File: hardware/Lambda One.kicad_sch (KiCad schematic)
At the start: 35 parts, among them IC1 DS1818, J1 Conn_01x02, SW1 SW_Push, U1 W65C816SxP, U12 74HC245, U3 ATF22LV10C, U8 74HC00, U9 74HC00, Y1 TFT680

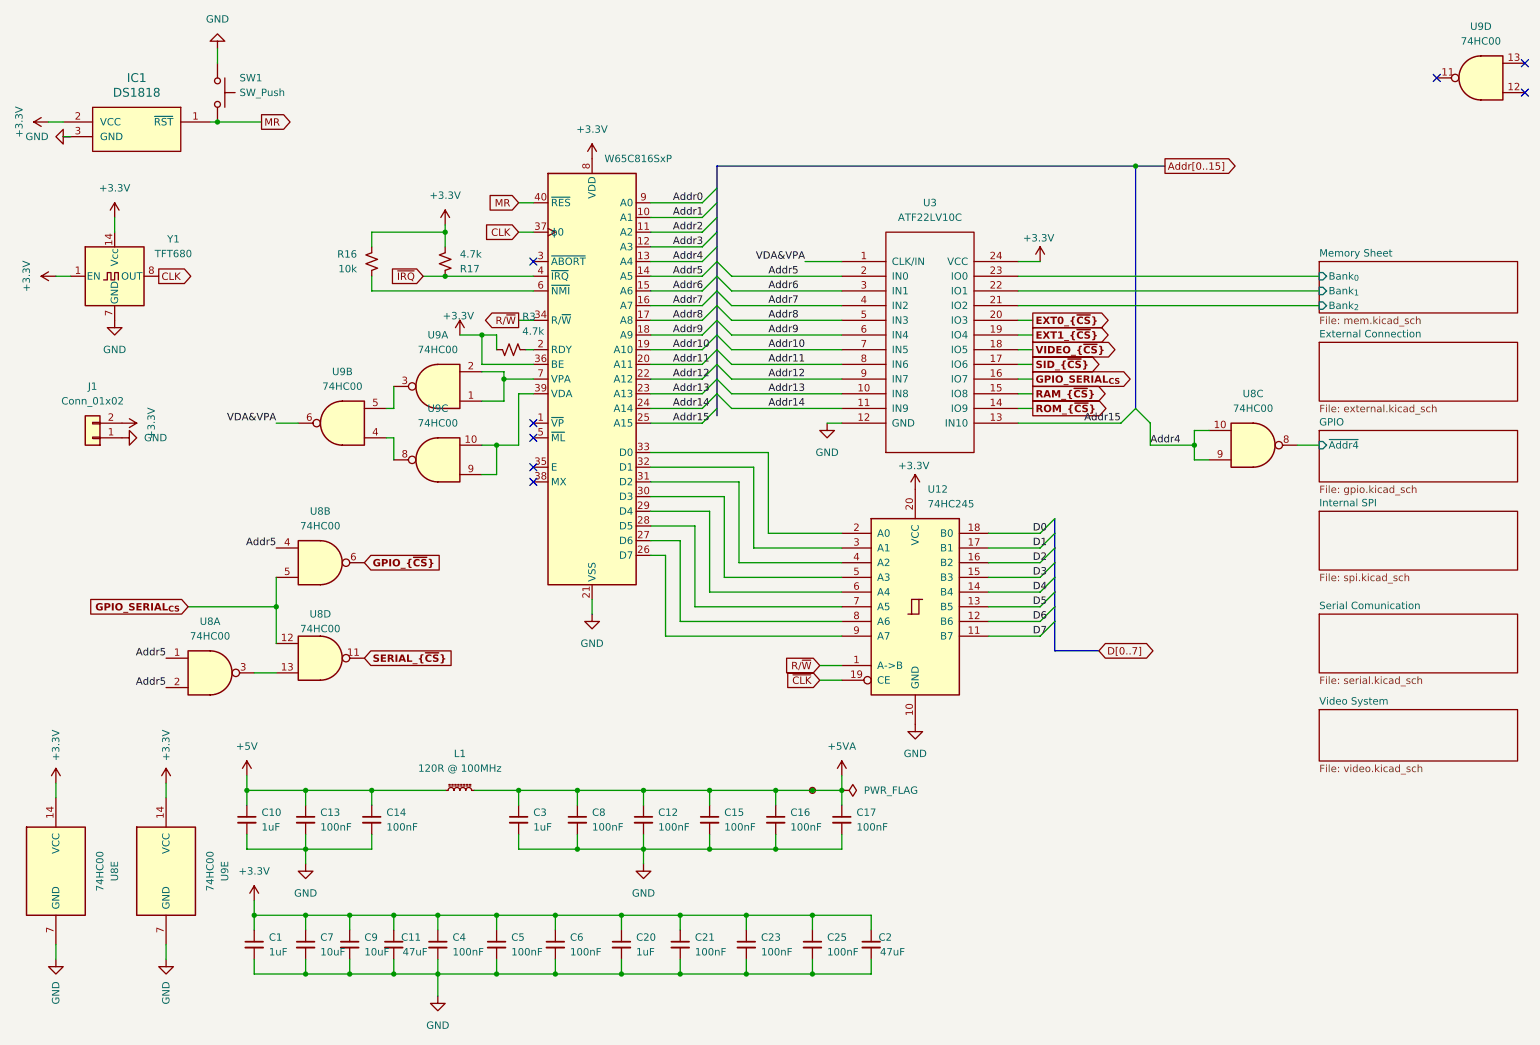
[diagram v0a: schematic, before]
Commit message: Add new categories for Video&Audio and Sound System in project configuration
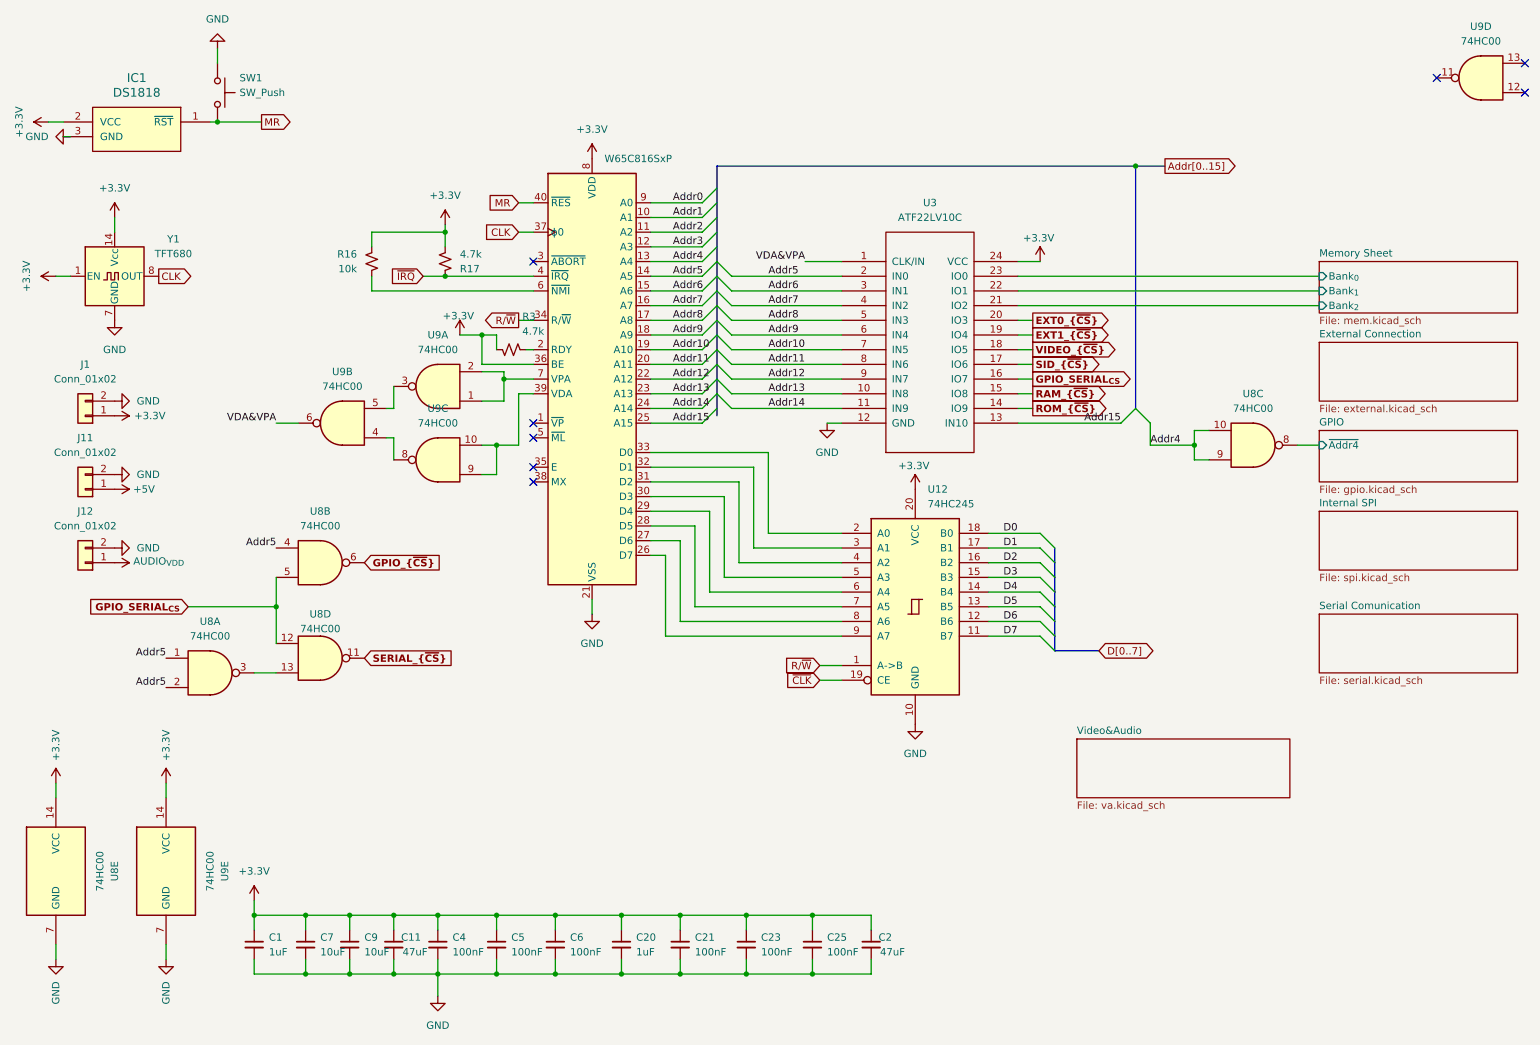
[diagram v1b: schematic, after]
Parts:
- removed C10, C3: 1uF, Capacitor_SMD:C_0603_1608Metric, symbol Device:C_Small
- removed C12, C13, C14, C15, C16, C17, C8: 100nF, Capacitor_SMD:C_0603_1608Metric, symbol Device:C_Small
- removed L1: 120R @ 100MHz, Inductor_SMD:L_0603_1608Metric, symbol Device:L_Ferrite_Small
- removed TP1: TestPoint_Small, TestPoint:TestPoint_Pad_D1.5mm, symbol Connector:TestPoint_Small
- added J11, J12: Conn_01x02, Connector_JST:JST_XH_B2B-XH-A_1x02_P2.50mm_Vertical, symbol Connector_Generic:Conn_01x02
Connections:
- net +3.3V: now also J1.1 (Pin_1); no longer J1.2 (Pin_2)
- net +5V: now also J11.1 (Pin_1)
- net GND: now also J1.2 (Pin_2), J11.2 (Pin_2), J12.2 (Pin_2); no longer J1.1 (Pin_1)
- new net AUDIO_{VDD}: J12.1 (Pin_1)
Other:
- removed sheet Video System
- added sheet Video&Audio (va.kicad_sch)
- moved on the sheet: J1

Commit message: Moved connection to external connections
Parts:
- removed J1, J11, J12: Conn_01x02, Connector_JST:JST_XH_B2B-XH-A_1x02_P2.50mm_Vertical, symbol Connector_Generic:Conn_01x02

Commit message: PCD DESIGN
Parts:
- ADDR1: renamed from U3; footprint ATF22V10C-10PU:24-DIP -> Package_DIP:DIP-24_W7.62mm
- renumbered U1 to CPU1, U12 to CPU_DB1
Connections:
- net Addr12: now also ADDR1.13 (IN10); no longer ADDR1.9 (IN7)
- net Addr13: now also ADDR1.11 (IN9); no longer ADDR1.10 (IN8)
- net Addr14: now also ADDR1.10 (IN8); no longer ADDR1.11 (IN9)
- net Addr15: now also ADDR1.9 (IN7); no longer ADDR1.13 (IN10)
- net RAM_{~{CS}}: now also ADDR1.14 (IO9); no longer ADDR1.15 (IO8)
- net ROM_{~{CS}}: now also ADDR1.15 (IO8); no longer ADDR1.14 (IO9)
- net at U9.10, U9.9: now also CPU1.7 (VPA); no longer CPU1.39 (VDA)
- net at U9.8: now also U9.5; no longer U9.4
- net at U9.1, U9.2: now also CPU1.39 (VDA); no longer CPU1.7 (VPA)
- net at U9.3: now also U9.4; no longer U9.5
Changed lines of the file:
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@@
 		)
 	)
+	(label "Addr13"
+		(at 146.05 86.36 0)
+		(effects
+			(font
+				(size 1.27 1.27)
+			)
+			(justify left bottom)
+		)
+	)
 	(label "Addr10"
 		(at 129.54 76.2 0)
@@
 		)
 	)
-	(label "Addr15"
+	(label "Addr12"
 		(at 200.66 88.9 0)
 		(effects
@@
 		)
 	)
-	(label "Addr13"
+	(label "Addr14"
 		(at 146.05 83.82 0)
 		(effects
@@
 		)
 	)
-	(label "Addr12"
-		(at 146.05 81.28 0)
+	(label "D7"
+		(at 186.69 125.73 0)
 		(effects
 			(font
@@
 		)
 	)
-	(label "D7"
-		(at 186.69 125.73 0)
+	(label "Addr15"
+		(at 146.05 81.28 0)
 		(effects
 			(font
@@
 		)
 	)
-	(label "Addr14"
-		(at 146.05 86.36 0)
-		(effects
-			(font
-				(size 1.27 1.27)
-			)
-			(justify left bottom)
-		)
-	)
 	(label "Addr9"
 		(at 129.54 73.66 0)
@@
 		)
 	)
-	(global_label "ROM_{~{CS}}"
-		(shape output)
-		(at 191.77 86.36 0)
+	(global_label "GPIO_{~{CS}}"
+		(shape input)
+		(at 76.2 113.03 0)
 		(fields_autoplaced yes)
 		(effects
@@
 		)
 		(property "Intersheetrefs" "${INTERSHEET_REFS}"
-			(at 200.8415 86.36 0)
+			(at 86.1709 113.03 0)
 			(effects
 				(font
@@
 		)
 	)
-	(global_label "GPIO_{~{CS}}"
+	(global_label "R{slash}~{W}"
 		(shape input)
-		(at 76.2 113.03 0)
+		(at 154.94 130.81 180)
 		(fields_autoplaced yes)
 		(effects
 			(font
 				(size 1.27 1.27)
-				(thickness 0.254)
-				(bold yes)
 			)
-			(justify left)
+			(justify right)
 		)
 		(property "Intersheetrefs" "${INTERSHEET_REFS}"
-			(at 86.1709 113.03 0)
+			(at 147.9029 130.81 0)
 			(effects
 				(font
 					(size 1.27 1.27)
 				)
-				(justify left)
+				(justify right)
 				(hide yes)
 			)
 		)
 	)
-	(global_label "R{slash}~{W}"
+	(global_label "SERIAL_{~{CS}}"
 		(shape input)
-		(at 154.94 130.81 180)
+		(at 76.2 129.54 0)
 		(fields_autoplaced yes)
 		(effects
 			(font
 				(size 1.27 1.27)
+				(thickness 0.254)
+				(bold yes)
 			)
-			(justify right)
+			(justify left)
 		)
 		(property "Intersheetrefs" "${INTERSHEET_REFS}"
-			(at 147.9029 130.81 0)
+			(at 88.0456 129.54 0)
 			(effects
 				(font
 					(size 1.27 1.27)
 				)
-				(justify right)
+				(justify left)
 				(hide yes)
 			)
 		)
 	)
-	(global_label "SERIAL_{~{CS}}"
-		(shape input)
-		(at 76.2 129.54 0)
+	(global_label "ROM_{~{CS}}"
+		(shape output)
+		(at 191.77 83.82 0)
 		(fields_autoplaced yes)
 		(effects
@@
 		)
 		(property "Intersheetrefs" "${INTERSHEET_REFS}"
-			(at 88.0456 129.54 0)
+			(at 200.8415 83.82 0)
 			(effects
 				(font
@@
 	(global_label "RAM_{~{CS}}"
 		(shape output)
-		(at 191.77 83.82 0)
+		(at 191.77 86.36 0)
 		(fields_autoplaced yes)
 		(effects
@@
 		)
 		(property "Intersheetrefs" "${INTERSHEET_REFS}"
-			(at 200.5996 83.82 0)
+			(at 200.5996 86.36 0)
 			(effects
 				(font
@@
 	(symbol
 		(lib_id "74xx:74HC00")
-		(at 88.9 95.25 180)
+		(at 88.9 82.55 180)
 		(unit 3)
 		(exclude_from_sim no)
@@
 		(fields_autoplaced yes)
 		(property "Reference" "U9"
-			(at 88.9083 86.36 0)
+			(at 88.9083 73.66 0)
 			(effects
 				(font
@@
 		)
 		(property "Value" "74HC00"
-			(at 88.9083 88.9 0)
+			(at 88.9083 76.2 0)
 			(effects
 				(font
@@
 		)
 		(property "Footprint" "Package_DIP:DIP-14_W7.62mm"
-			(at 88.9 95.25 0)
+			(at 88.9 82.55 0)
 			(effects
 				(font
@@
 		)
 		(property "Datasheet" "http://www.ti.com/lit/gpn/sn74hc00"
-			(at 88.9 95.25 0)
+			(at 88.9 82.55 0)
 			(effects
 				(font
@@
 		)
 		(property "Description" "quad 2-input NAND gate"
-			(at 88.9 95.25 0)
+			(at 88.9 82.55 0)
 			(effects
 				(font
@@
 		(dnp no)
 		(fields_autoplaced yes)
-		(property "Reference" "U12"
+		(property "Reference" "CPU_DB1"
 			(at 173.5933 100.33 0)
 			(effects
@@
 			(project "Lambda One"
 				(path "/73ea9964-373f-4fdc-b03e-f532cf836c0d"
-					(reference "U12")
+					(reference "CPU_DB1")
 					(unit 1)
 				)
@@
 	)
 	(symbol
-		(lib_id "74xx:74HC00")
-		(at 88.9 82.55 180)
-		(unit 1)
-		(exclude_from_sim no)
-		(in_bom yes)
-		(on_board yes)
-		(dnp no)
-		(fields_autoplaced yes)
-		(property "Reference" "U9"
-			(at 88.9083 73.66 0)
-			(effects
-				(font
-					(size 1.27 1.27)
-				)
-			)
-		)
-		(property "Value" "74HC00"
-			(at 88.9083 76.2 0)
-			(effects
-				(font
-					(size 1.27 1.27)
-				)
-			)
-		)
-		(property "Footprint" "Package_DIP:DIP-14_W7.62mm"
-			(at 88.9 82.55 0)
-			(effects
-				(font
-					(size 1.27 1.27)
-				)
-				(hide yes)
-			)
-		)
-		(property "Datasheet" "http://www.ti.com/lit/gpn/sn74hc00"
-			(at 88.9 82.55 0)
-			(effects
-				(font
-					(size 1.27 1.27)
-				)
-				(hide yes)
-			)
-		)
-		(property "Description" "quad 2-input NAND gate"
-			(at 88.9 82.55 0)
-			(effects
-				(font
-					(size 1.27 1.27)
-				)
-				(hide yes)
-			)
-		)
-		(pin "1"
-		)
-		(pin "2"
-		)
-		(pin "14"
-		)
-		(pin "13"
-		)
-		(pin "5"
-		)
-		(pin "7"
-		)
-		(pin "6"
-		)
-		(pin "3"
-		)
-		(pin "9"
-		)
-		(pin "12"
-		)
-		(pin "8"
-		)
-		(pin "11"
-		)
-		(pin "4"
-		)
-		(pin "10"
-		)
-		(instances
-			(project "Lambda One"
-				(path "/73ea9964-373f-4fdc-b03e-f532cf836c0d"
-					(reference "U9")
-					(unit 1)
-				)
-			)
-		)
-	)
-	(symbol
 		(lib_id "power:+3.3V")
 		(at 22.86 63.5 90)
@@
 		(dnp no)
 		(fields_autoplaced yes)
-		(property "Reference" "U3"
+		(property "Reference" "ADDR1"
 			(at 173.99 50.8 0)
 			(effects
@@
 			)
 		)
-		(property "Footprint" "ATF22V10C-10PU:24-DIP"
+		(property "Footprint" "Package_DIP:DIP-24_W7.62mm"
 			(at 173.99 74.93 0)
 			(effects
@@
 			(project "Lambda One"
 				(path "/73ea9964-373f-4fdc-b03e-f532cf836c0d"
-					(reference "U3")
+					(reference "ADDR1")
 					(unit 1)
 				)
@@
 	)
 	(symbol
+		(lib_id "74xx:74HC00")
+		(at 88.9 95.25 180)
+		(unit 1)
+		(exclude_from_sim no)
+		(in_bom yes)
+		(on_board yes)
+		(dnp no)
+		(property "Reference" "U9"
+			(at 89.154 88.138 0)
+			(effects
+				(font
+					(size 1.27 1.27)
+				)
+			)
+		)
+		(property "Value" "74HC00"
+			(at 88.9 90.17 0)
+			(effects
+				(font
+					(size 1.27 1.27)
+				)
+			)
+		)
+		(property "Footprint" "Package_DIP:DIP-14_W7.62mm"
+			(at 88.9 95.25 0)
+			(effects
+				(font
+					(size 1.27 1.27)
+				)
+				(hide yes)
+			)
+		)
+		(property "Datasheet" "http://www.ti.com/lit/gpn/sn74hc00"
+			(at 88.9 95.25 0)
+			(effects
+				(font
+					(size 1.27 1.27)
+				)
+				(hide yes)
+			)
+		)
+		(property "Description" "quad 2-input NAND gate"
+			(at 88.9 95.25 0)
+			(effects
+				(font
+					(size 1.27 1.27)
+				)
+				(hide yes)
+			)
+		)
+		(pin "1"
+		)
+		(pin "2"
+		)
+		(pin "14"
+		)
+		(pin "13"
+		)
+		(pin "5"
+		)
+		(pin "7"
+		)
+		(pin "6"
+		)
+		(pin "3"
+		)
+		(pin "9"
+		)
+		(pin "12"
+		)
+		(pin "8"
+		)
+		(pin "11"
+		)
+		(pin "4"
+		)
+		(pin "10"
+		)
+		(instances
+			(project "Lambda One"
+				(path "/73ea9964-373f-4fdc-b03e-f532cf836c0d"
+					(reference "U9")
+					(unit 1)
+				)
+			)
+		)
+	)
+	(symbol
 		(lib_id "power:GND")
 		(at 25.4 39.37 270)
@@
 		(dnp no)
 		(fields_autoplaced yes)
-		(property "Reference" "U1"
+		(property "Reference" "CPU1"
 			(at 117.7133 40.64 0)
 			(effects
@@
 			(project "Lambda One"
 				(path "/73ea9964-373f-4fdc-b03e-f532cf836c0d"
-					(reference "U1")
+					(reference "CPU1")
 					(unit 1)
 				)

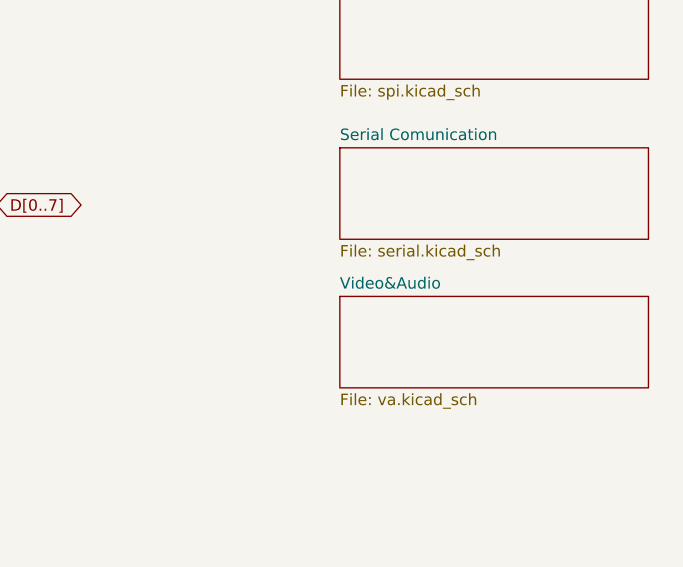
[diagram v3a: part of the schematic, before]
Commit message: Removed old VPU
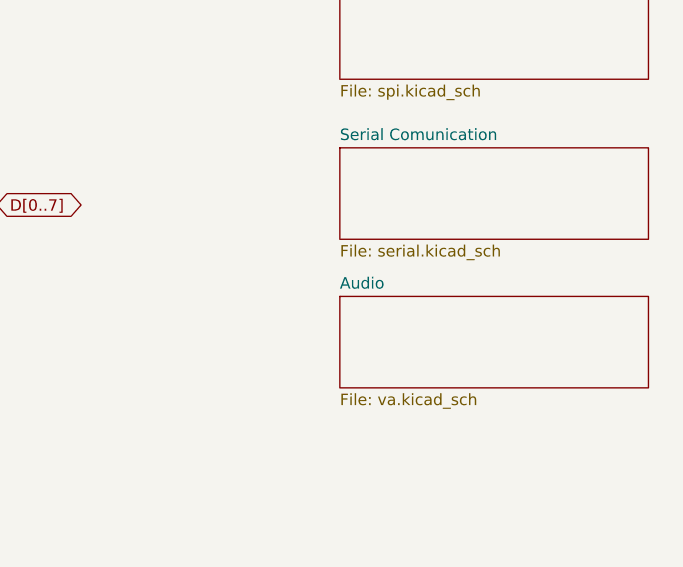
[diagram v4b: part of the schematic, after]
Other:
- sheet Video&Audio renamed Audio
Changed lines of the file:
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@@
 			(color 0 0 0 0.0000)
 		)
-		(property "Sheetname" "Video&Audio"
+		(property "Sheetname" "Audio"
 			(at 241.3 137.7184 0)
 			(effects
